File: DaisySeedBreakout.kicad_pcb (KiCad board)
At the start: 2 copper layers, 41.1 x 66 mm, 154 parts, among them J10 Conn_01x03, J11 Conn_01x03, J12 Conn_01x03, J13 Conn_01x03, J14 Conn_01x03, J15 Conn_02x08, J16 STX-3000, J17 STX-3000, J19 STX-3000, J2 Conn_02x08, J3 STX-3000, J4 5027740891, J5 Conn_02x08, J6 Conn_01x03, J7 Conn_01x03, J8 Conn_01x03, J9 Conn_01x03, U1 TCA6424ARGJR, U2 H11L1M, U4 SN74AHCT1G125_DCK_5, U5 MAX9814

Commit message: adding 3d models
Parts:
- moved J10 5.08 mm to (121.9, 61.0)
- moved J11 5.08 mm to (119.4, 38.1)
- moved J12 5.08 mm to (119.4, 45.7)
- moved J13 5.08 mm to (119.4, 53.3)
- moved J14 5.08 mm to (119.4, 61.0)
- moved J6 5.08 mm to (121.9, 38.1)
- moved J8 5.08 mm to (121.9, 45.7)
- moved J9 5.08 mm to (121.9, 53.3)
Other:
- board size 41.1 x 66 mm -> 46.2 x 66 mm
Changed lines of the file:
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@@
   )
   (footprint "Connector_PinHeader_2.54mm:PinHeader_1x03_P2.54mm_Vertical" (layer "F.Cu")
-    (at 124.46 60.96)
+    (at 119.38 60.96)
     (descr "Through hole straight pin header, 1x03, 2.54mm pitch, single row")
     (tags "Through hole pin header THT 1x03 2.54mm single row")
@@
   )
   (footprint "Connector_PinHeader_2.54mm:PinHeader_1x03_P2.54mm_Vertical" (layer "F.Cu")
-    (at 127 38.1)
+    (at 121.92 38.1)
     (descr "Through hole straight pin header, 1x03, 2.54mm pitch, single row")
     (tags "Through hole pin header THT 1x03 2.54mm single row")
@@
   )
   (footprint "Connector_PinHeader_2.54mm:PinHeader_1x03_P2.54mm_Vertical" (layer "F.Cu")
-    (at 127 60.96)
+    (at 121.92 60.96)
     (descr "Through hole straight pin header, 1x03, 2.54mm pitch, single row")
     (tags "Through hole pin header THT 1x03 2.54mm single row")
@@
   )
   (footprint "Connector_PinHeader_2.54mm:PinHeader_1x03_P2.54mm_Vertical" (layer "F.Cu")
-    (at 124.46 53.34)
+    (at 119.38 53.34)
     (descr "Through hole straight pin header, 1x03, 2.54mm pitch, single row")
     (tags "Through hole pin header THT 1x03 2.54mm single row")
@@
   )
   (footprint "Connector_PinHeader_2.54mm:PinHeader_1x03_P2.54mm_Vertical" (layer "F.Cu")
-    (at 124.46 45.72)
+    (at 119.38 45.72)
     (descr "Through hole straight pin header, 1x03, 2.54mm pitch, single row")
     (tags "Through hole pin header THT 1x03 2.54mm single row")
@@
   )
   (footprint "Connector_PinHeader_2.54mm:PinHeader_1x03_P2.54mm_Vertical" (layer "F.Cu")
-    (at 124.46 38.1)
+    (at 119.38 38.1)
     (descr "Through hole straight pin header, 1x03, 2.54mm pitch, single row")
     (tags "Through hole pin header THT 1x03 2.54mm single row")
@@
   )
   (footprint "Connector_PinHeader_2.54mm:PinHeader_1x03_P2.54mm_Vertical" (layer "F.Cu")
-    (at 127 53.34)
+    (at 121.92 53.34)
     (descr "Through hole straight pin header, 1x03, 2.54mm pitch, single row")
     (tags "Through hole pin header THT 1x03 2.54mm single row")
@@
   )
   (footprint "Connector_PinHeader_2.54mm:PinHeader_1x03_P2.54mm_Vertical" (layer "F.Cu")
-    (at 127 45.72)
+    (at 121.92 45.72)
     (descr "Through hole straight pin header, 1x03, 2.54mm pitch, single row")
     (tags "Through hole pin header THT 1x03 2.54mm single row")
@@
     )
   )
-  (gr_rect (start 118.11 34.798) (end 159.258 100.838)
+  (gr_rect (start 115.57 34.798) (end 161.798 100.838)
     (stroke (width 0.2) (type default)) (fill none) (layer "Edge.Cuts"))
   (segment (start 137.150347 55.24275) (end 137.150347 52.1613) (width 0.25) (layer "B.Cu") (net 0))

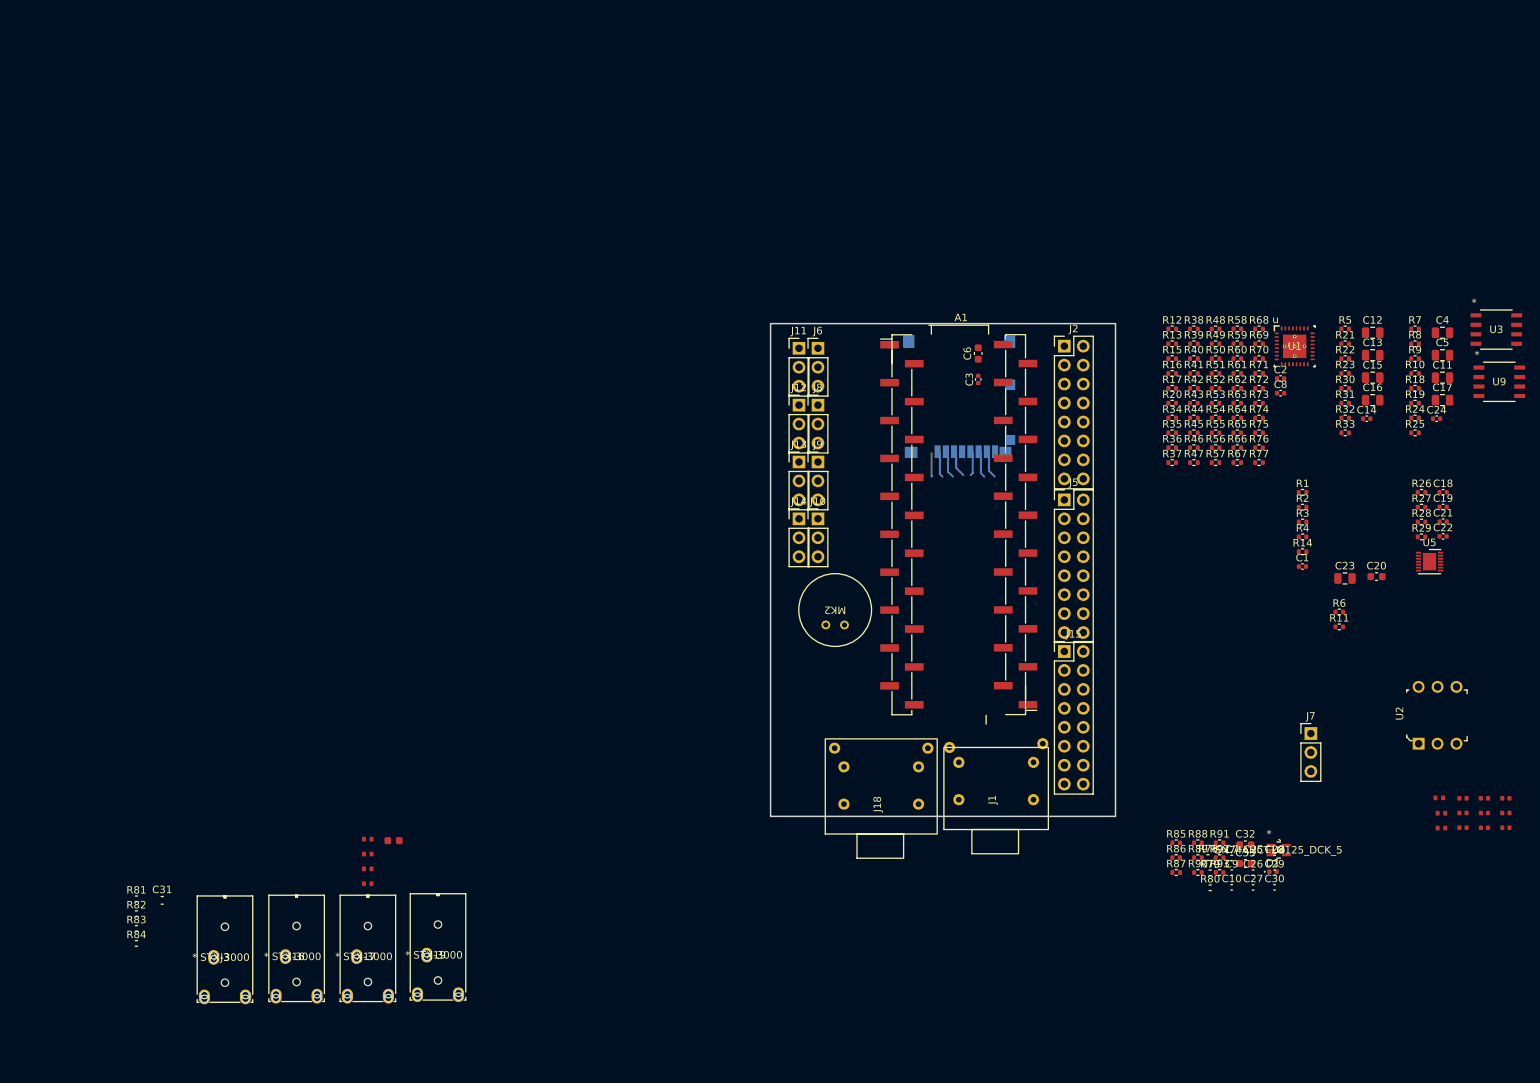
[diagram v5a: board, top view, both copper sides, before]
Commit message: adding mono connectors, CV, and gate as well
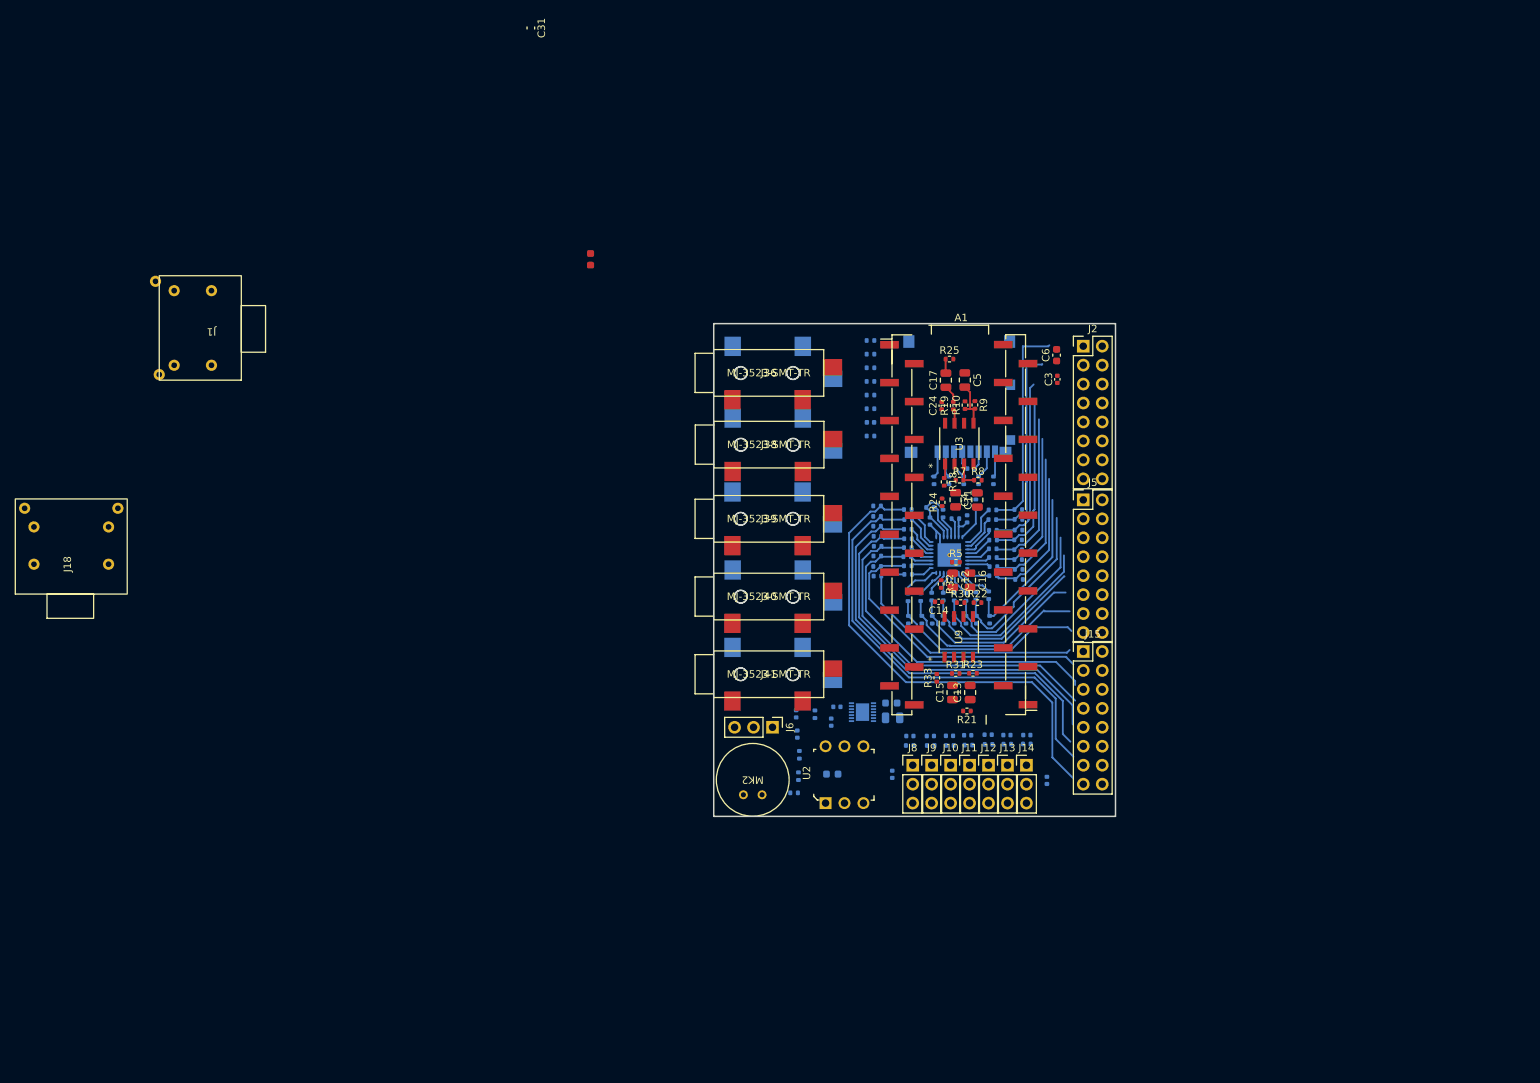
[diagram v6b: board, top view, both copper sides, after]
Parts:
- removed C33: 0.1uF, Capacitor_SMD:C_0603_1608Metric
- removed J16, J17, J19, J3: STX-3000, Ultralibrarian:STX-3000_KYC
- removed J7: Conn_01x03, Connector_PinHeader_2.54mm:PinHeader_1x03_P2.54mm_Vertical
- removed R92: 220, Resistor_SMD:R_0402_1005Metric
- removed R93: SPARE, Resistor_SMD:R_0402_1005Metric
- removed U4: SN74AHCT1G125_DCK_5, Ultralibrarian:DCK5
- added J36: MJ-3523-SMT-TR, SurfaceMountAudiofootprints:MJ-3523-SMT-TR, F.Cu at (115.3, 41.4)
- added J37: MJ-3523-SMT-TR, SurfaceMountAudiofootprints:MJ-3523-SMT-TR, B.Cu at (115.3, 41.4)
- added J38: MJ-3523-SMT-TR, SurfaceMountAudiofootprints:MJ-3523-SMT-TR, F.Cu at (115.3, 51.0)
- added J39: MJ-3523-SMT-TR, SurfaceMountAudiofootprints:MJ-3523-SMT-TR, F.Cu at (115.3, 61.0)
- added J40: MJ-3523-SMT-TR, SurfaceMountAudiofootprints:MJ-3523-SMT-TR, F.Cu at (115.3, 71.4)
- added J41: MJ-3523-SMT-TR, SurfaceMountAudiofootprints:MJ-3523-SMT-TR, F.Cu at (115.3, 81.8)
- added J42: MJ-3523-SMT-TR, SurfaceMountAudiofootprints:MJ-3523-SMT-TR, B.Cu at (115.3, 51.1)
- added J43: MJ-3523-SMT-TR, SurfaceMountAudiofootprints:MJ-3523-SMT-TR, B.Cu at (115.3, 61.0)
- added J44: MJ-3523-SMT-TR, SurfaceMountAudiofootprints:MJ-3523-SMT-TR, B.Cu at (115.3, 71.4)
- added J45: MJ-3523-SMT-TR, SurfaceMountAudiofootprints:MJ-3523-SMT-TR, B.Cu at (115.3, 81.8)
- C1, C18, C19, C2, C20, C21, C22, C23, C26, C29, C30, C32, C8, D1, R1, R11, R12, R13, R14, R15, R16, R17, R2, R20, R26, R27, R28, R29, R3, R34, R35, R36, R37, R38, R39, R4, R40, R41, R42, R43, R44, R45, R46, R47, R48, R49, R50, R51, R52, R53, R54, R55, R56, R57, R58, R59, R6, R60, R61, R62, R63, R64, R65, R66, R67, R68, R69, R70, R71, R72, R73, R74, R75, R76, R77, R78, R79, R80, R81, R82, R83, R84, R85, R86, R87, R88, R89, U1, U5: moved to B.Cu
- C10, C25, C27, C28, C7, C9: value 0.1uF -> SPARE; moved to B.Cu
- R90: value 220 -> 10; moved to B.Cu
- R91: value SPARE -> 33; moved to B.Cu
- moved C31 126.9 mm to (83.4, -4.83), turned to -90 degrees
- moved J1 122.7 mm to (40.6, 35.4), turned to 180 degrees
- moved R84 122.3 mm to (149.9, 91.1)
- moved R83 119.3 mm to (147.3, 91.2)
- moved R82 116.4 mm to (144.8, 91.2)
- moved R81 113.4 mm to (142.1, 91.3)
- moved J18 113.2 mm to (21.8, 67.0)
- moved R27 92.4 mm to (118.7, 97.7)
- moved R26 91.8 mm to (119.3, 95.5), turned to -90 degrees
- moved C21 91.1 mm to (119.2, 89.8), turned to -90 degrees
- moved C19 91.0 mm to (119.0, 87.1), turned to 90 degrees
- moved R28 89.0 mm to (119.4, 92.6), turned to -90 degrees
- moved C18 87.6 mm to (123.7, 88.2), turned to -90 degrees
- moved R29 84.7 mm to (121.5, 87.1), turned to 90 degrees
- moved C22 84.4 mm to (124.5, 86.2)
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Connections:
- J1 pad 1A: unconnected-(J1-Pad1A) -> GND
- J1 pad 2A: unconnected-(J1-Pad2A) -> Net-(J1-Pad2A)
- J1 pad 5A: unconnected-(J1-Pad5A) -> Net-(J1-Pad5A)
- R90 pad 1: +5V_ISO -> /MIDI_UART_TX
- R90 pad 2: Net-(R90-Pad2) -> Net-(J1-Pad2A)
- R91 pad 2: Net-(R91-Pad2) -> Net-(J1-Pad5A)
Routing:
- net /I2C 24 GPIO/C7: track 0.00 -> 64.2 mm
- net /I2C 24 GPIO/C6: track 0.00 -> 59.6 mm
- net /I2C 24 GPIO/C5: track 0.00 -> 55.6 mm
- net /I2C 24 GPIO/C4: track 0.00 -> 51.7 mm
- net /I2C 24 GPIO/C3: track 0.00 -> 47.1 mm
- net /I2C 24 GPIO/C2: track 0.00 -> 44.1 mm
- net /I2C 24 GPIO/C1: track 0.00 -> 39.5 mm
- net /I2C 24 GPIO/C0: track 0.00 -> 35.0 mm
- net /I2C 24 GPIO/A0: track 0.00 -> 28.4 mm
- net /I2C 24 GPIO/B7: track 0.00 -> 27.3 mm
- net /I2C 24 GPIO/A1: track 0.00 -> 26.4 mm
- net /I2C 24 GPIO/B6: track 0.00 -> 25.9 mm
- net /I2C 24 GPIO/B5: track 0.00 -> 24.6 mm
- net /I2C 24 GPIO/B3: track 0.00 -> 23.8 mm
- net /I2C 24 GPIO/B2: track 0.00 -> 23.5 mm
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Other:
- board size 46.2 x 66 mm -> 53.8 x 66 mm

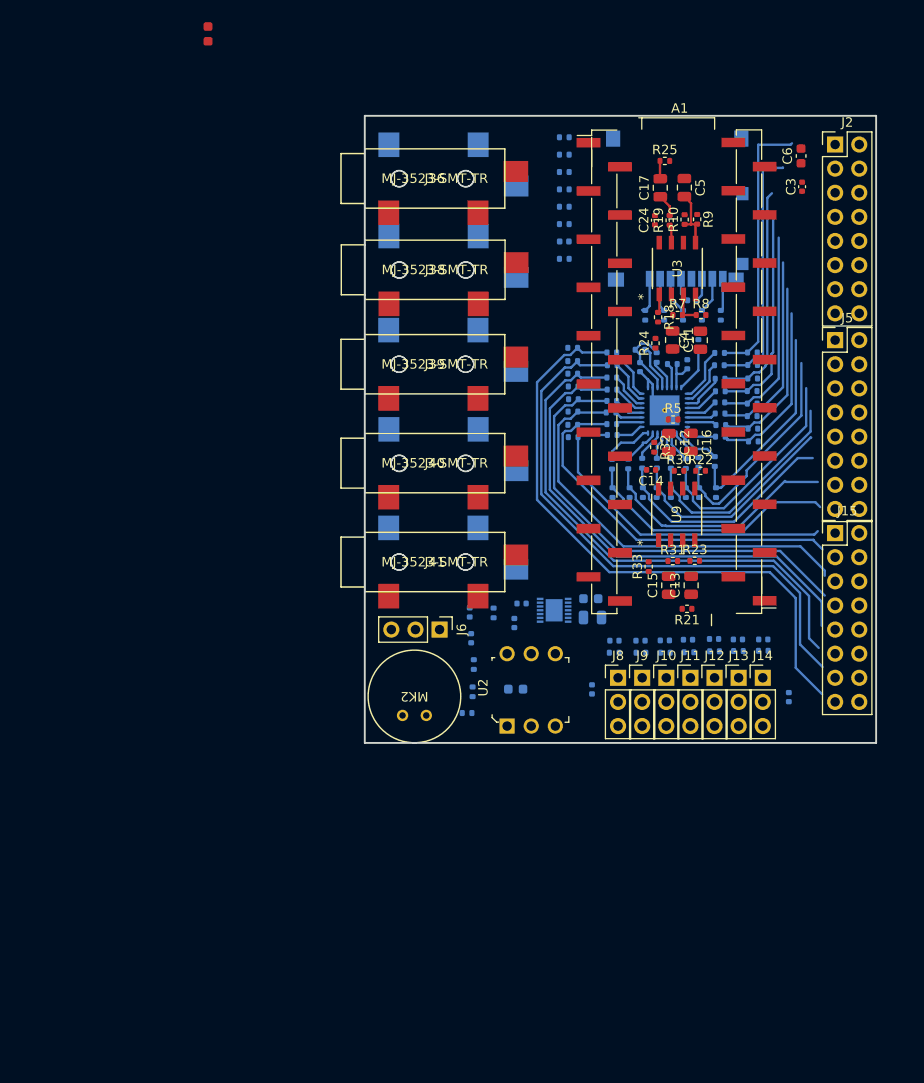
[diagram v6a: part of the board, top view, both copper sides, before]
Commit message: update design to use more headers.  Need to figure out easy way to integrate connectors in modular but easy to use way without dangling wires
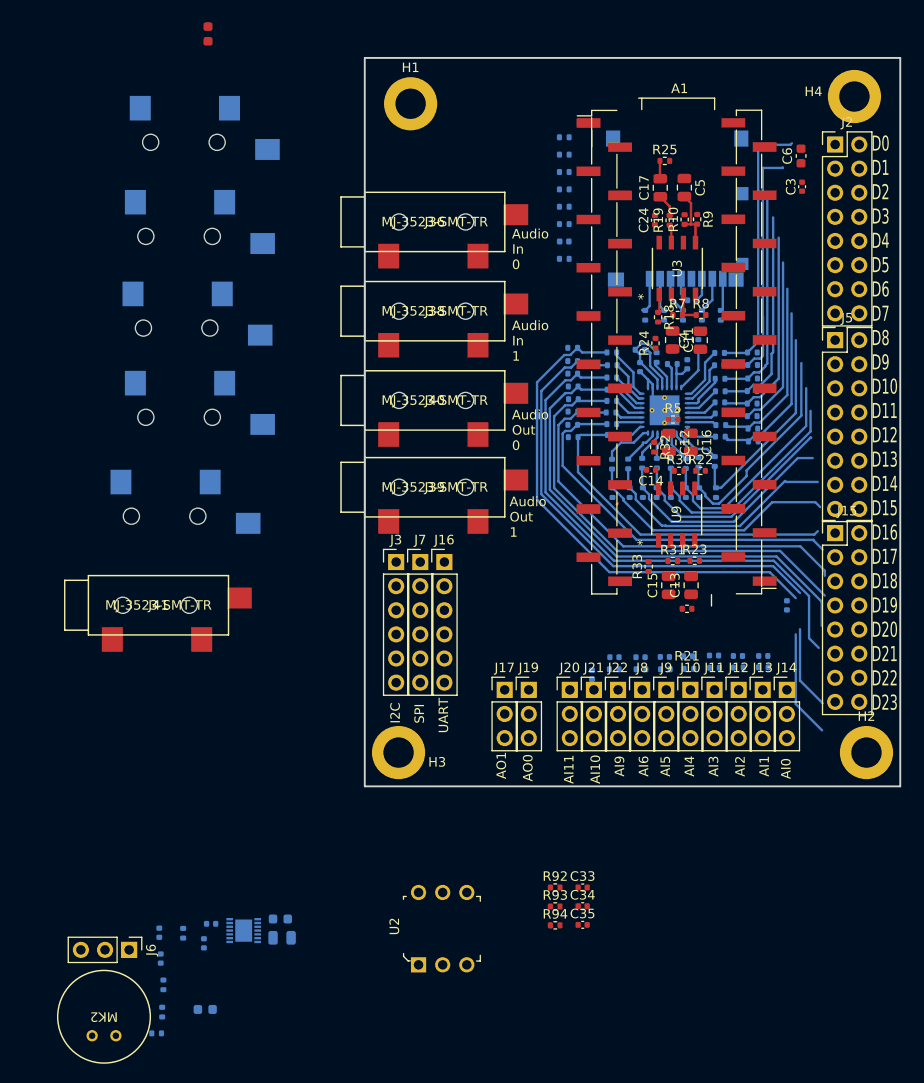
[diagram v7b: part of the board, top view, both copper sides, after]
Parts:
- added C33: SPARE, Capacitor_SMD:C_0402_1005Metric, F.Cu at (130.9, 116.1)
- added C34: SPARE, Capacitor_SMD:C_0402_1005Metric, F.Cu at (130.9, 118.0)
- added C35: SPARE, Capacitor_SMD:C_0402_1005Metric, F.Cu at (130.9, 120.0)
- added H1: MountingHole, MountingHole:MountingHole_3.2mm_M3_DIN965_Pad, F.Cu at (112.8, 33.5)
- added H2: MountingHole, MountingHole:MountingHole_3.2mm_M3_DIN965_Pad, F.Cu at (160.8, 101.9)
- added H3: MountingHole, MountingHole:MountingHole_3.2mm_M3_DIN965_Pad, F.Cu at (111.5, 101.9)
- added H4: MountingHole, MountingHole:MountingHole_3.2mm_M3_DIN965_Pad, F.Cu at (159.5, 32.8)
- added J16: Conn_01x06, Ultralibrarian:PinHeader_1x06_P2.54mm_Vertical_Female, F.Cu at (116.3, 81.8)
- added J17: Conn_01x03, Ultralibrarian:PinHeader_1x03_P2.54mm_Vertical_Female, F.Cu at (122.7, 95.2)
- added J19: Conn_01x03, Ultralibrarian:PinHeader_1x03_P2.54mm_Vertical_Female, F.Cu at (125.2, 95.2)
- added J20: Conn_01x03, Ultralibrarian:PinHeader_1x03_P2.54mm_Vertical_Female, F.Cu at (129.5, 95.2)
- added J21: Conn_01x03, Ultralibrarian:PinHeader_1x03_P2.54mm_Vertical_Female, F.Cu at (132.1, 95.2)
- added J22: Conn_01x03, Ultralibrarian:PinHeader_1x03_P2.54mm_Vertical_Female, F.Cu at (134.6, 95.2)
- added J3: Conn_01x06, Ultralibrarian:PinHeader_1x06_P2.54mm_Vertical_Female, F.Cu at (111.3, 81.8)
- added J7: Conn_01x06, Ultralibrarian:PinHeader_1x06_P2.54mm_Vertical_Female, F.Cu at (113.8, 81.8)
- added R92: 1k, Resistor_SMD:R_0402_1005Metric, F.Cu at (128.0, 116.1)
- added R93: 1k, Resistor_SMD:R_0402_1005Metric, F.Cu at (128.0, 118.1)
- added R94: 1k, Resistor_SMD:R_0402_1005Metric, F.Cu at (128.0, 120.0)
- J10, J11, J12, J13, J14, J8, J9: footprint Connector_PinHeader_2.54mm:PinHeader_1x03_P2.54mm_Vertical -> Ultralibrarian:PinHeader_1x03_P2.54mm_Vertical_Female
- J15, J2, J5: footprint Connector_PinHeader_2.54mm:PinHeader_2x08_P2.54mm_Vertical -> Ultralibrarian:PinHeader_2x08_P2.54mm_Vertical_Female
- moved C23 47.0 mm to (99.2, 121.4)
- moved C22 47.0 mm to (91.8, 119.9)
- moved MK2 47.0 mm to (80.5, 129.7)
- moved R27 47.0 mm to (86.0, 131.4)
- moved R28 47.0 mm to (86.7, 126.3)
- moved U5 47.0 mm to (95.2, 120.6)
- moved C18 47.0 mm to (91.0, 121.9)
- moved C19 47.0 mm to (86.3, 120.8)
- moved C20 47.0 mm to (99.1, 119.4)
- moved C21 47.0 mm to (86.5, 123.5)
- moved C32 47.0 mm to (91.1, 128.9)
- moved J6 47.0 mm to (83.1, 122.6)
- moved R26 47.0 mm to (86.6, 129.2)
- moved R29 47.0 mm to (88.8, 120.9)
- moved J44 42.8 mm to (89.2, 37.6)
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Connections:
- A1 pad 31: unconnected-(A1-SAI2_MCLK-Pad31) -> /AI9
- A1 pad 32: unconnected-(A1-SAI2_SD_B-Pad32) -> /AI10
- A1 pad 35: unconnected-(A1-SAI2_SCK-Pad35) -> /AI11
- C29 pad 1: +5V_ISO -> +3.3V
- C30 pad 1: +5V_ISO -> +3.3V
- J10 pad 2: +5V_ISO -> +3.3V
- J11 pad 2: +5V_ISO -> +3.3V
- J12 pad 2: +5V_ISO -> +3.3V
- J13 pad 2: +5V_ISO -> +3.3V
- J14 pad 2: +5V_ISO -> +3.3V
- J8 pad 2: +5V_ISO -> +3.3V
- J9 pad 2: +5V_ISO -> +3.3V
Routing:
- net GND: track 7.89 -> 19.2 mm
- net /I2C 24 GPIO/C7: track 64.2 -> 53.0 mm
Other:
- board size 53.8 x 66 mm -> 56.4 x 76.7 mm
- board text added: "AI0"
- board text added: "AI1"
- board text added: "AI10"
- board text added: "AI11"
- board text added: "AI2"
- board text added: "AI3"
- board text added: "AI4"
- board text added: "AI5"
- board text added: "AI6"
- board text added: "AI9"
- board text added: "AO0"
- board text added: "AO1"
- board text added: "Audio In 0"
- board text added: "Audio In 1"
- board text added: "Audio Out 0"
- board text added: "Audio Out 1"
- board text added: "D0 D1 D2 D3 D4 D5 D6 D7 D8 D9 D10 D11 D12 D13 D14 D15 D16 D17 D18 D19 D20 D21 D22 D23"
- board text added: "I2C"
- board text added: "SPI"
- board text added: "UART"
